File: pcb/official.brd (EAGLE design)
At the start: 114.3 x 55.5 mm, 16 parts, among them P1 DEV_CLP-150, P8 DEV_1X40

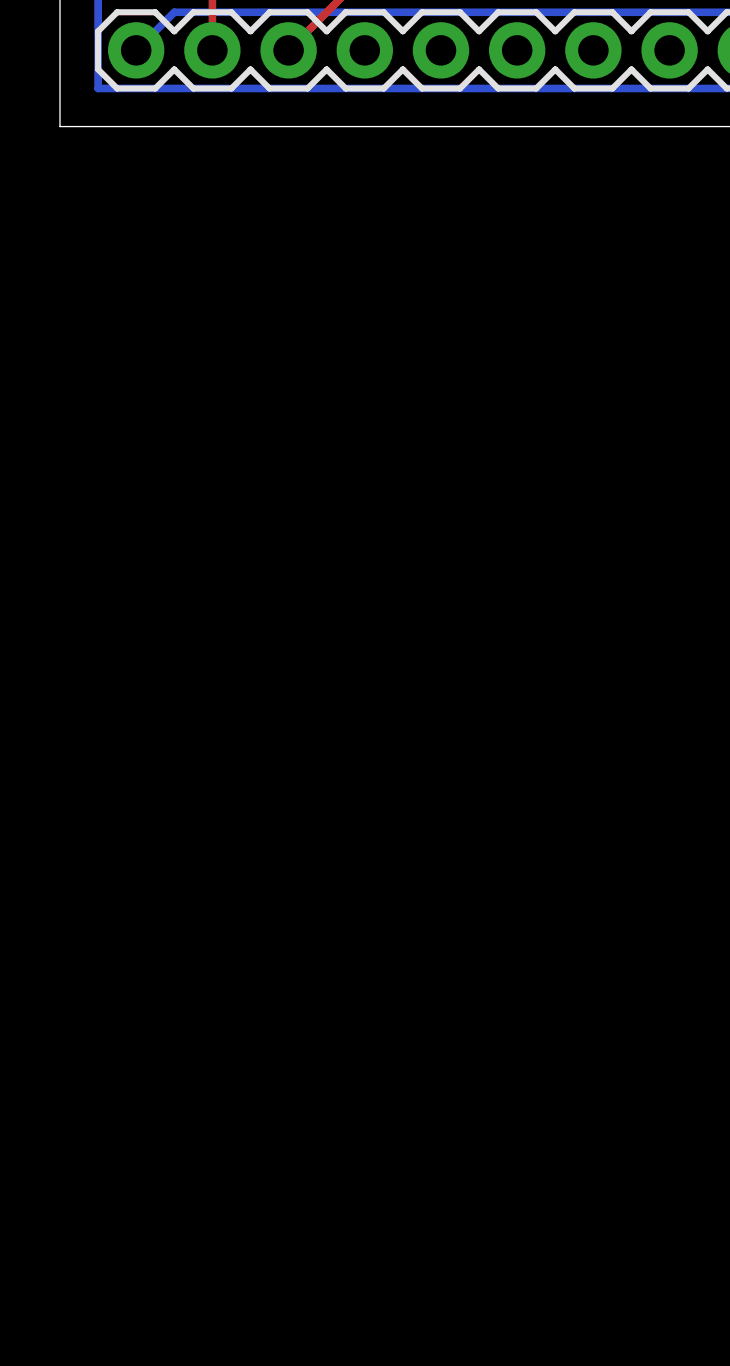
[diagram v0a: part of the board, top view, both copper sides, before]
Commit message: Added sound amp to pcb design file
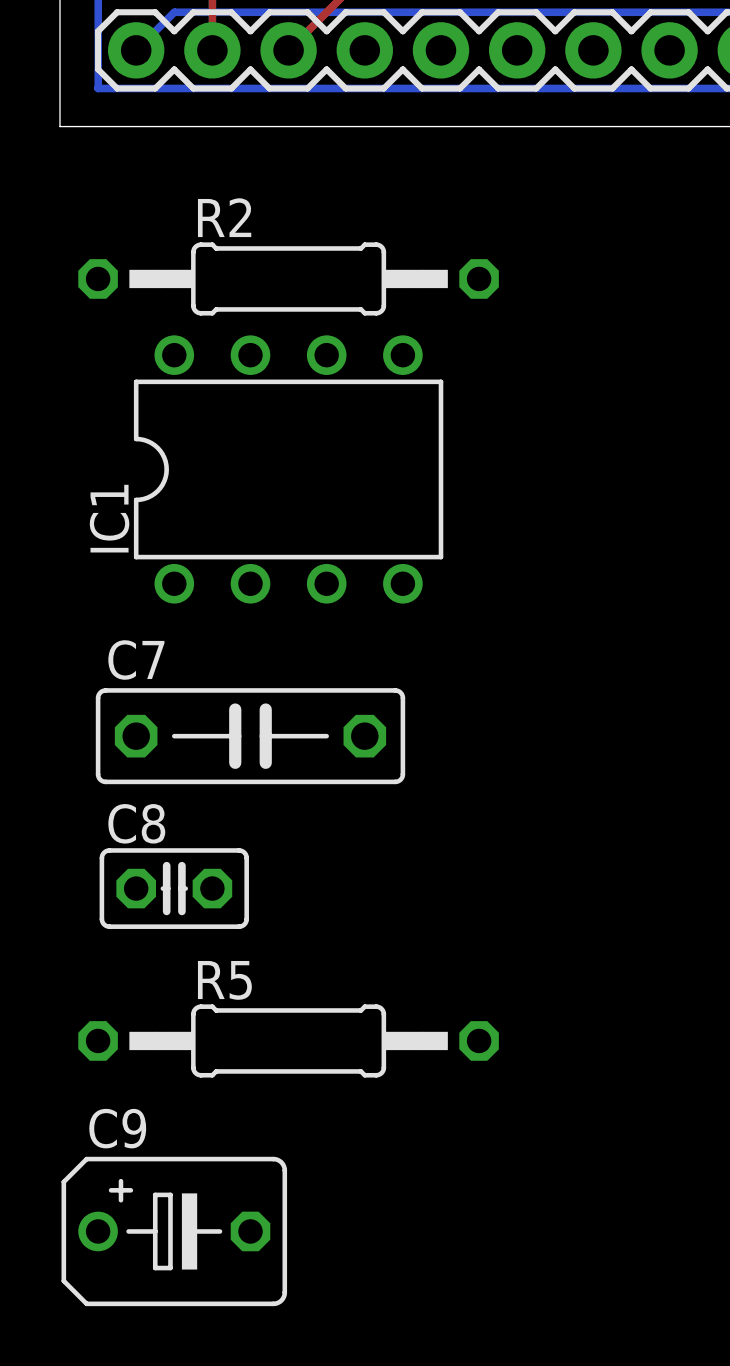
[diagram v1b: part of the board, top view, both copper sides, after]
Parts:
- added C7: (no value), rcl:C075-032X103
- added C8: (no value), rcl:C025-025X050
- added C9: (no value), rcl:B45181B
- added IC1: LM386N-4, linear:DIL08
- added R2, R5: (no value), rcl:0207/12
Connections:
- new net N$2: C7.1, IC1.3, R5.1
- new net N$4: C8.2, R2.2
- new net N$5: C8.1, C9.+, IC1.5
- new net N$6: IC1.6
- new net SPKR: C9.-, P8.31
- net ADC7: no longer P8.31
- net DACOUT1: now also C7.2
- net GND: now also IC1.2, IC1.4, R2.1, R5.2
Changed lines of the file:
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@@
 <element name="R6" library="rcl" package="0309/12" value="200" x="138.43" y="60.96"/>
 <element name="R7" library="rcl" package="0309/12" value="10k" x="137.16" y="83.82"/>
+<element name="R2" library="rcl" package="0207/12" value="" x="53.34" y="39.37"/>
+<element name="IC1" library="linear" package="DIL08" value="LM386N-4" x="53.34" y="33.02"/>
+<element name="C7" library="rcl" package="C075-032X103" value="" x="52.07" y="24.13"/>
+<element name="C8" library="rcl" package="C025-025X050" value="" x="49.53" y="19.05"/>
+<element name="R5" library="rcl" package="0207/12" value="" x="53.34" y="13.97"/>
+<element name="C9" library="rcl" package="B45181B" value="" x="49.53" y="7.62"/>
 </elements>
 <signals>
@@
 <signal name="DACOUT1">
 <contactref element="P1" pad="P$46"/>
+<contactref element="C7" pad="2"/>
+<wire x1="55.88" y1="24.13" x2="97.155" y2="98.51" width="0" layer="19" extent="1-1"/>
 </signal>
 <signal name="ADC10">
@@
 <signal name="ADC7">
 <contactref element="P1" pad="P$82"/>
-<contactref element="P8" pad="31"/>
-<wire x1="71.12" y1="46.99" x2="74.295" y2="98.51" width="0" layer="19" extent="1-1"/>
 </signal>
 <signal name="MSS_GP_IO_11">
@@
 <wire x1="107.95" y1="76.2" x2="107.95" y2="73.66" width="0.254" layer="1"/>
 <wire x1="110.49" y1="78.74" x2="107.95" y2="76.2" width="0.254" layer="1"/>
+<contactref element="IC1" pad="2"/>
+<contactref element="IC1" pad="4"/>
+<contactref element="R5" pad="2"/>
+<contactref element="R2" pad="1"/>
+<wire x1="46.99" y1="39.37" x2="53.34" y2="54.2925" width="0" layer="19" extent="1-1"/>
+<wire x1="52.07" y1="29.21" x2="46.99" y2="39.37" width="0" layer="19" extent="1-1"/>
+<wire x1="57.15" y1="29.21" x2="52.07" y2="29.21" width="0" layer="19" extent="1-1"/>
+<wire x1="59.69" y1="13.97" x2="57.15" y2="29.21" width="0" layer="19" extent="1-1"/>
 </signal>
 <signal name="LMOTOR">
@@
 <wire x1="144.78" y1="67.31" x2="142.24" y2="69.85" width="0.254" layer="16"/>
 </signal>
+<signal name="N$2">
+<contactref element="IC1" pad="3"/>
+<contactref element="C7" pad="1"/>
+<contactref element="R5" pad="1"/>
+<wire x1="48.26" y1="24.13" x2="54.61" y2="29.21" width="0" layer="19" extent="1-1"/>
+<wire x1="46.99" y1="13.97" x2="48.26" y2="24.13" width="0" layer="19" extent="1-1"/>
+</signal>
+<signal name="N$4">
+<contactref element="R2" pad="2"/>
+<contactref element="C8" pad="2"/>
+<wire x1="50.8" y1="19.05" x2="59.69" y2="39.37" width="0" layer="19" extent="1-1"/>
+</signal>
+<signal name="N$5">
+<contactref element="IC1" pad="5"/>
+<contactref element="C8" pad="1"/>
+<contactref element="C9" pad="+"/>
+<wire x1="48.26" y1="19.05" x2="57.15" y2="36.83" width="0" layer="19" extent="1-1"/>
+<wire x1="46.99" y1="7.62" x2="48.26" y2="19.05" width="0" layer="19" extent="1-1"/>
+</signal>
+<signal name="N$6">
+<contactref element="IC1" pad="6"/>
+</signal>
+<signal name="SPKR">
+<contactref element="P8" pad="31"/>
+<contactref element="C9" pad="-"/>
+<wire x1="52.07" y1="7.62" x2="71.12" y2="46.99" width="0" layer="19" extent="1-1"/>
+</signal>
 </signals>

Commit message: Better pcb
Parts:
- removed C1, C2, C3, C4, C5, C6: (no value), SparkFun:0603-CAP
- removed IC1: LM386N-4, linear:DIL08
- removed LM219: (no value), ic-package:SOCKET-14
- removed P8: DEV_1X40, EECS370:1X40
- removed VOLT_REG: REG1117F, burr-brown:DD-3
- added C10, C11, C12, C15: (no value), rcl:B45181B
- added C13: (no value), rcl:C075-032X103
- added C14: (no value), rcl:C025-025X050
- added COMPARATOR: (no value), ic-package:SOCKET-14
- added OPAMP: LM386N-4, linear:DIL08
- added P11: DEV_1X40, EECS370:1X40
- added R8: 750, rcl:0309/12
- added R9: 10, rcl:0309/12
- added U$1: (no value), umich:UMICH
- added VREG: 7806T, linear:TO220H
- C7: device rcl:C075-032X103 -> rcl:B45181B
- C8: device rcl:C025-025X050 -> rcl:B45181B
- moved R6 137.8 mm to (8.89, 14.0)
- moved H-BRIDGE1 98.6 mm to (5.08, 21.6), turned to 90 degrees
- moved R7 86.4 mm to (101.6, 5.08)
- moved R3 81.7 mm to (81.3, 19.1)
- moved R4 76.5 mm to (81.3, 16.5)
- moved C9 72.1 mm to (119.4, 25.4), turned to 90 degrees
- moved R1 67.3 mm to (102.9, 15.2), turned to 270 degrees
- moved P1 66.6 mm to (71.3, 33.9), turned to 0 degrees
- moved C8 65.1 mm to (114.3, 25.4), turned to 90 degrees
- moved C7 57.2 mm to (109.2, 25.4), turned to 90 degrees
- moved R5 33.1 mm to (25.4, 31.8)
- moved R2 28.4 mm to (25.4, 34.3), turned to 180 degrees
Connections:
- removed net 5V: H-BRIDGE1.11, H-BRIDGE1.9, LM219.11, R1.2, R3.1, R4.1, R6.1, VOLT_REG.2
- removed net GND: H-BRIDGE1.1, H-BRIDGE1.15, H-BRIDGE1.8, IC1.2, IC1.4, LM219.3, LM219.6, LM219.8, R2.1, R5.2, VOLT_REG.1
- new net ADC11: P1.P$90
- new net ADC9: P1.P$86
- new net MSS_GPIO_5: P11.39
- new net MSS_GPIO_6: P11.40
- new net N$1: H-BRIDGE1.13, R9.2
- net 12.8V: no longer P8.39
- net 7.2V: now also VREG.1; no longer P8.38, VOLT_REG.3
- net ADC0: no longer P8.35
- net ADC1: no longer P8.36
- net ADC4: no longer P8.33
- net ADC5: no longer P8.34
- net ADC6: no longer P8.37
- net ADC8: no longer P8.32
- net AGND: now also P1.P$88, P1.P$92, P1.P$94
- net DACOUT1: now also C13.2; no longer C7.2
- net DGND: now also C10.-, C11.-, C12.-, C7.-, C8.-, C9.-, COMPARATOR.3, COMPARATOR.6, COMPARATOR.8, H-BRIDGE1.1, H-BRIDGE1.15, H-BRIDGE1.8, OPAMP.2, OPAMP.4, P1.P$96, P11.9, R2.1, R5.2, VREG.2; no longer C1.2, C2.2, C3.2, C4.2, C5.2, C6.2, P8.20, P8.3, P8.40
- net F2-200-IO_0: now also P11.30; no longer H-BRIDGE1.6
- net F2-200-IO_1: now also P11.31; no longer P8.29
- net F2-200-IO_2: now also P11.32; no longer P8.30, R7.1
- net F2-200-IO_3: now also P11.33, R7.1; no longer H-BRIDGE1.5
- net F2-200-IO_4: now also H-BRIDGE1.6; no longer H-BRIDGE1.7
- net F2-200-IO_5: now also H-BRIDGE1.5; no longer P8.28
- net F2-200-IO_6: now also H-BRIDGE1.7; no longer H-BRIDGE1.10
- net F2-200-IO_7: now also H-BRIDGE1.10; no longer H-BRIDGE1.12
- net F2-200-IO_8: now also H-BRIDGE1.12; no longer P8.27
- net LMOTOR: now also P11.24; no longer P8.21
- net LSERVO: now also P11.26, R9.1; no longer H-BRIDGE1.13, P8.23
- net MSS_GP_IO_0: now also P11.35, R8.2; no longer P8.4
- net MSS_GP_IO_1: now also COMPARATOR.12, R1.1; no longer P8.5
- net MSS_GP_IO_10: now also P11.18; no longer P8.14
- net MSS_GP_IO_11: now also P11.19; no longer P8.15
- net MSS_GP_IO_12: now also P11.20; no longer P8.16
- net MSS_GP_IO_13: now also P11.21; no longer P8.17
- net MSS_GP_IO_14: now also P11.22; no longer P8.18
- net MSS_GP_IO_15: now also P11.23; no longer P8.19
- net MSS_GP_IO_2: now also P11.36; no longer LM219.12, R1.1
- net MSS_GP_IO_3: now also P11.37; no longer P8.7
- net MSS_GP_IO_4: now also P11.38; no longer P8.8
- net MSS_GP_IO_5: no longer P8.9
- net MSS_GP_IO_6: no longer P8.10
- net MSS_GP_IO_7: now also P11.15; no longer P8.11
- net MSS_GP_IO_8: now also P11.16; no longer P8.12
- net MSS_GP_IO_9: now also P11.17; no longer P8.13
- net N$2: now also C13.1, OPAMP.3; no longer C7.1, IC1.3
- net N$3: now also COMPARATOR.5; no longer LM219.5
- net N$4: now also C14.2; no longer C8.2
- net N$5: now also C14.1, C15.+, OPAMP.5; no longer C8.1, C9.+, IC1.5
- net N$6: now also OPAMP.6; no longer IC1.6
- net REFS_IN: now also COMPARATOR.4, P11.28, R3.2; no longer P8.26, R6.2
- net REFS_OUT: now also P11.29, R6.2; no longer LM219.4, P8.25, R3.2
- net RMOTOR: now also P11.25; no longer P8.22
- net RSERVO: now also P11.27; no longer P8.24
- net SPKR: now also C15.-, P11.34; no longer C9.-, P8.31
- net VDD3.3: now also C10.+, C11.+, C12.+, P1.P$100, P1.P$98, P11.14; no longer C4.1, C5.1, C6.1, P8.2
- net VDD5: now also C7.+, C8.+, C9.+, COMPARATOR.11, H-BRIDGE1.11, H-BRIDGE1.9, P11.1, P11.4, R1.2, R3.1, R4.1, R6.1, R8.1, VREG.3; no longer C1.1, C2.1, C3.1, P8.1
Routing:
- net DGND: track 182.2 -> 0.00 mm
- net F2-200-IO_2: track 138.4 -> 0.00 mm
- net 5V: track 137.5 -> 0.00 mm
- net GND: track 122.6 -> 0.00 mm
- net VDD3.3: track 91.6 -> 0.00 mm
- net 12.8V: track 90.7 -> 0.00 mm
- net REFS_IN: track 76.7 -> 0.00 mm
- net REFS_OUT: track 75.1 -> 0.00 mm, vias 1 -> 0
- net VDD5: track 58.0 -> 0.00 mm
- net LSERVO: track 42.8 -> 0.00 mm
- net RSERVO: track 42.0 -> 0.00 mm
- net RMOTOR: track 38.6 -> 0.00 mm
- net N$3: track 36.9 -> 0.00 mm
- net MSS_GP_IO_2: track 35.6 -> 0.00 mm
- net LMOTOR: track 34.1 -> 0.00 mm
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- added copper zone on layer 16, net N$7
- added copper zone on layer 1, net N$8
- added copper zone on layer 1, net VDD3.3
- added copper zone on layer 1, net VDD5
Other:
- board size 114.3 x 55.5 mm -> 122.9 x 36.9 mm
- board text added: "3.3V"
- board text added: "5V"
- board text added: "9"
- board text added: "DGND"
- board text added: "GC_SIG"
- board text added: "GND"
- board text added: "IR_IN"
- board text added: "IR_OUT"
- board text added: "LCD_SIG"
- board text added: "LMOTOR"
- board text added: "LSERVO"
- board text added: "MAG_S"
- board text added: "MSS10"
- board text added: "MSS11"
- board text added: "MSS12"
- board text added: "MSS13"
- board text added: "MSS14"
- board text added: "MSS15"
- board text added: "MSS7"
- board text added: "MSS8"
- board text added: "MSS9"
- board text added: "Nov. 25 '13 Christen"
- board text added: "REF_IN"
- board text added: "REF_OUT"
- board text added: "RMOTOR"
- board text added: "RSERVO"
- board text added: "SPKR"
- board text added: "UMKARTS EECS 373 Car Board"
- board text added: "V12.8"
- board text added: "V3.3"
- board text added: "V5"
- board text added: "V7.2"
- board text added: "XB_CTS"
- board text added: "XB_RTR"
- board text added: "XB_RTS"
- board text added: "XB_RX"
- board text added: "XB_TX"

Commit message: Rough draft
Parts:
- removed R6: 200, rcl:0309/12
- removed R7: 10k, rcl:0309/12
- removed R8: 750, rcl:0309/12
- added R10: 200, rcl:0309/12
- added R11: 10k, rcl:0309/12
- added R12: 750, rcl:0309/12
- moved C10 105.6 mm to (14.0, 24.1)
- moved C11 105.6 mm to (8.89, 24.1)
- moved C12 105.6 mm to (3.81, 24.1)
- moved C7 105.6 mm to (3.81, 31.8)
- moved C8 105.6 mm to (8.89, 31.8)
- moved C9 105.6 mm to (14.0, 31.8)
- moved C13 94.1 mm to (114.3, 25.4), turned to 0 degrees
- moved VREG 91.8 mm to (36.8, 1.27), turned to 180 degrees
- moved R2 90.4 mm to (114.3, 17.8), turned to 0 degrees
- moved R5 89.5 mm to (114.3, 21.6), turned to 180 degrees
- moved C14 73.7 mm to (99.1, 15.2), turned to 0 degrees
- moved OPAMP 68.7 mm to (101.6, 22.9), turned to 90 degrees
- moved R9 64.1 mm to (72.4, 19.1), turned to 270 degrees
- moved C15 62.2 mm to (106.7, 14.0)
- moved H-BRIDGE1 55.9 mm to (61.0, 21.6), turned to 0 degrees
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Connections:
- net 12.8V: now also P11.8
- net 7.2V: now also P11.5
- net DGND: now also P11.10, P11.11, P11.12, P11.6, P11.7
- net F2-200-IO_0: now also P11.21; no longer P11.30
- net F2-200-IO_1: now also P11.22; no longer P11.31
- net F2-200-IO_2: now also P11.23; no longer P11.32
- net F2-200-IO_3: now also P11.24, R11.1; no longer P11.33, R7.1
- net LMOTOR: now also P11.15; no longer P11.24
- net LSERVO: now also P11.17; no longer P11.26
- net MSS_GPIO_5: now also P11.30; no longer P11.39
- net MSS_GPIO_6: now also P11.31; no longer P11.40
- net MSS_GP_IO_0: now also P11.26, R12.2; no longer P11.35, R8.2
- net MSS_GP_IO_10: now also P11.35; no longer P11.18
- net MSS_GP_IO_11: now also P11.36; no longer P11.19
- net MSS_GP_IO_12: now also P11.37; no longer P11.20
- net MSS_GP_IO_13: now also P11.38; no longer P11.21
- net MSS_GP_IO_14: now also P11.39; no longer P11.22
- net MSS_GP_IO_15: now also P11.40; no longer P11.23
- net MSS_GP_IO_2: now also P11.27; no longer P11.36
- net MSS_GP_IO_3: now also P11.28; no longer P11.37
- net MSS_GP_IO_4: now also P11.29; no longer P11.38
- net MSS_GP_IO_7: now also P11.32; no longer P11.15
- net MSS_GP_IO_8: now also P11.33; no longer P11.16
- net MSS_GP_IO_9: now also P11.34; no longer P11.17
- net REFS_IN: now also P11.19; no longer P11.28
- net REFS_OUT: now also P11.20, R10.2; no longer P11.29, R6.2
- net RMOTOR: now also P11.16; no longer P11.25
- net RSERVO: now also P11.18; no longer P11.27
- net SPKR: now also P11.25; no longer P11.34
- net VDD3.3: now also P11.13, R11.2; no longer R7.2
- net VDD5: now also P11.2, P11.3, R10.1, R12.1; no longer R6.1, R8.1
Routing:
- net DGND: track 0.00 -> 275.2 mm, vias 0 -> 15
- net VDD5: track 0.00 -> 229.8 mm, vias 0 -> 2
- net VDD3.3: track 0.00 -> 152.1 mm, vias 0 -> 6
- net AGND: track 0.00 -> 82.4 mm, vias 0 -> 3
- net F2-200-IO_6: track 0.00 -> 81.3 mm, vias 0 -> 6
- net F2-200-IO_7: track 0.00 -> 62.6 mm, vias 0 -> 3
- net MSS_GP_IO_0: track 0.00 -> 55.0 mm, vias 0 -> 3
- net DACOUT1: track 0.00 -> 54.1 mm, vias 0 -> 1
- net MSS_GP_IO_1: track 0.00 -> 46.6 mm, vias 0 -> 1
- net N$4: track 0.00 -> 21.4 mm
- net N$5: track 0.00 -> 20.3 mm
- net F2-200-IO_5: track 0.00 -> 19.3 mm
- net F2-200-IO_4: track 0.00 -> 19.0 mm, vias 0 -> 3
- net F2-200-IO_3: track 0.00 -> 18.6 mm, vias 0 -> 1
- net N$2: track 0.00 -> 17.3 mm
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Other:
- board text removed: "3.3V"
- board text removed: "5V"

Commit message: New kyle resistor
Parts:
- added R6: (no value), rcl:0207/12
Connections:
- new net N$9: C13.2, R6.2
- net 12.8V: no longer P11.8
- net 7.2V: no longer P11.5
- net DACOUT1: now also R6.1; no longer C13.2
- net DGND: no longer P11.10, P11.11, P11.6, P11.7
- net VDD5: no longer P11.2, P11.3
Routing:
- net MSS_GP_IO_9: track 0.00 -> 156.6 mm, vias 0 -> 11
- net MSS_GP_IO_11: track 0.00 -> 130.2 mm, vias 0 -> 9
- net MSS_GP_IO_8: track 0.00 -> 124.2 mm, vias 0 -> 9
- net MSS_GP_IO_2: track 0.00 -> 112.1 mm, vias 0 -> 12
- net MSS_GP_IO_15: track 0.00 -> 110.8 mm, vias 0 -> 3
- net MSS_GP_IO_10: track 0.00 -> 102.1 mm, vias 0 -> 12
- net MSS_GP_IO_12: track 0.00 -> 96.7 mm, vias 0 -> 9
- net MSS_GP_IO_4: track 0.00 -> 95.4 mm, vias 0 -> 12
- net MSS_GP_IO_13: track 0.00 -> 95.2 mm, vias 0 -> 9
- net MSS_GP_IO_14: track 0.00 -> 93.2 mm, vias 0 -> 3
- net MSS_GP_IO_7: track 0.00 -> 81.7 mm, vias 0 -> 8
- net REFS_OUT: track 0.00 -> 80.7 mm, vias 0 -> 5
- net MSS_GP_IO_3: track 0.00 -> 77.6 mm, vias 0 -> 10
- net MSS_GP_IO_0: track 55.0 -> 124.6 mm, vias 3 -> 10
- net F2-200-IO_1: track 0.00 -> 57.5 mm, vias 0 -> 10
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
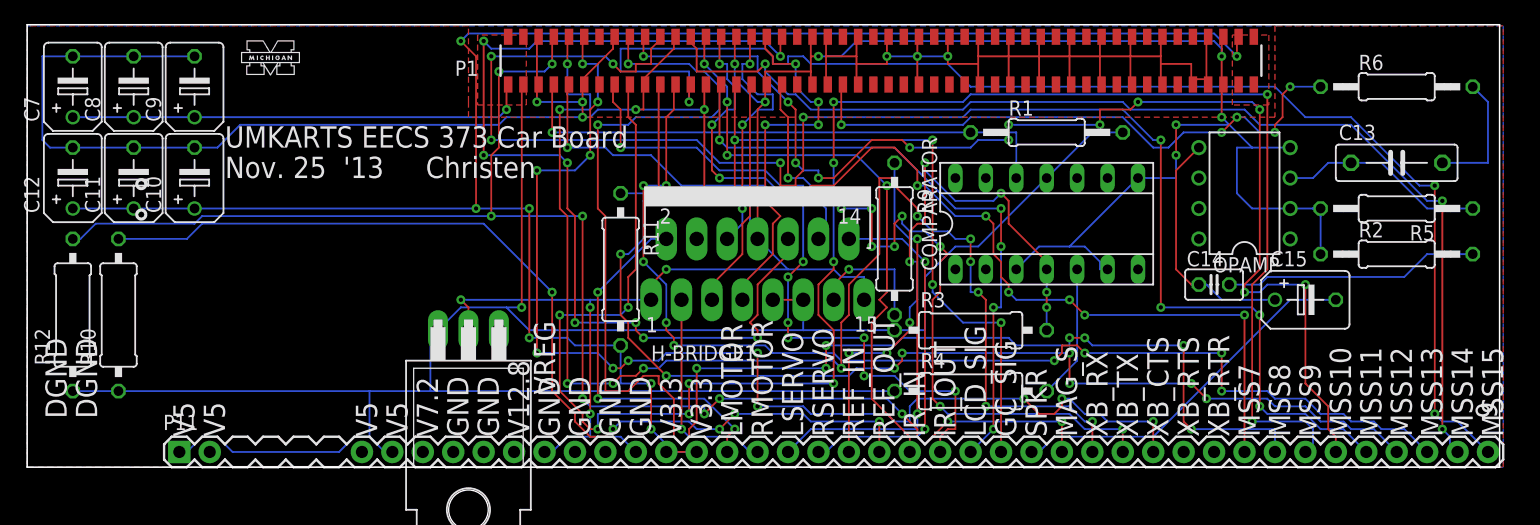
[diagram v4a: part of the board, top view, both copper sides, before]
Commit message: Added right resistors for comparator
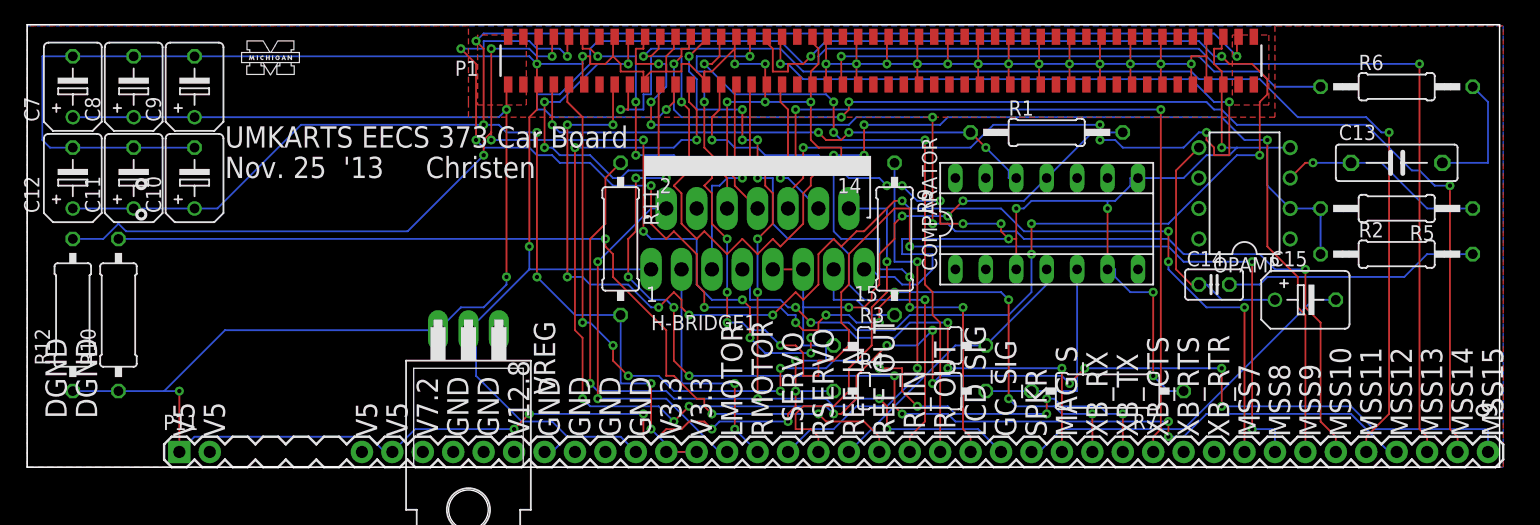
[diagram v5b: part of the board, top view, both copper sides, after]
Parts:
- added R7: 2.2k, rcl:0309/12
- moved R3 5.24 mm to (73.7, 10.2)
- moved R4 5.08 mm to (73.7, 6.35)
- moved H-BRIDGE1 2.54 mm to (61.0, 24.1)
- moved R11 2.54 mm to (49.5, 19.1)
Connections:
- net DGND: now also R7.1
- net N$3: now also R7.2
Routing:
- net F2-200-IO_6: track 31.6 -> 109.6 mm, vias 4 -> 7
- net MSS_GP_IO_9: track 156.6 -> 115.6 mm, vias 11 -> 6
- net MSS_GP_IO_11: track 130.2 -> 95.4 mm, vias 9 -> 2
- net MSS_GP_IO_13: track 95.2 -> 126.1 mm, vias 9 -> 2
- net REFS_IN: track 51.2 -> 23.6 mm, vias 8 -> 0
- net F2-200-IO_3: track 65.4 -> 87.7 mm, vias 5 -> 8
- net MSS_GP_IO_7: track 81.7 -> 103.3 mm, vias 8 -> 10
- net MSS_GP_IO_15: track 110.8 -> 129.1 mm, vias 3 -> 13
- net MSS_GP_IO_2: track 112.1 -> 98.0 mm
- net VDD5: track 229.8 -> 217.2 mm, vias 2 -> 14
- net MSS_GP_IO_10: track 102.1 -> 92.7 mm, vias 12 -> 6
- net F2-200-IO_7: track 83.8 -> 91.1 mm, vias 8 -> 6
- net N$3: track 11.2 -> 17.8 mm
- net MSS_GP_IO_0: track 124.6 -> 130.8 mm, vias 10 -> 13
- net DACOUT1: track 49.4 -> 43.4 mm, vias 5 -> 1
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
